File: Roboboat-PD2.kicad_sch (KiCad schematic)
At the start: 43 parts, among them J1 14.4V, J10 Motor, J11 Motor, J12 Motor, J13 Motor, J14 Motor, J15 Motor, J16 Motor, J17 GND TP, J2 PGOOD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

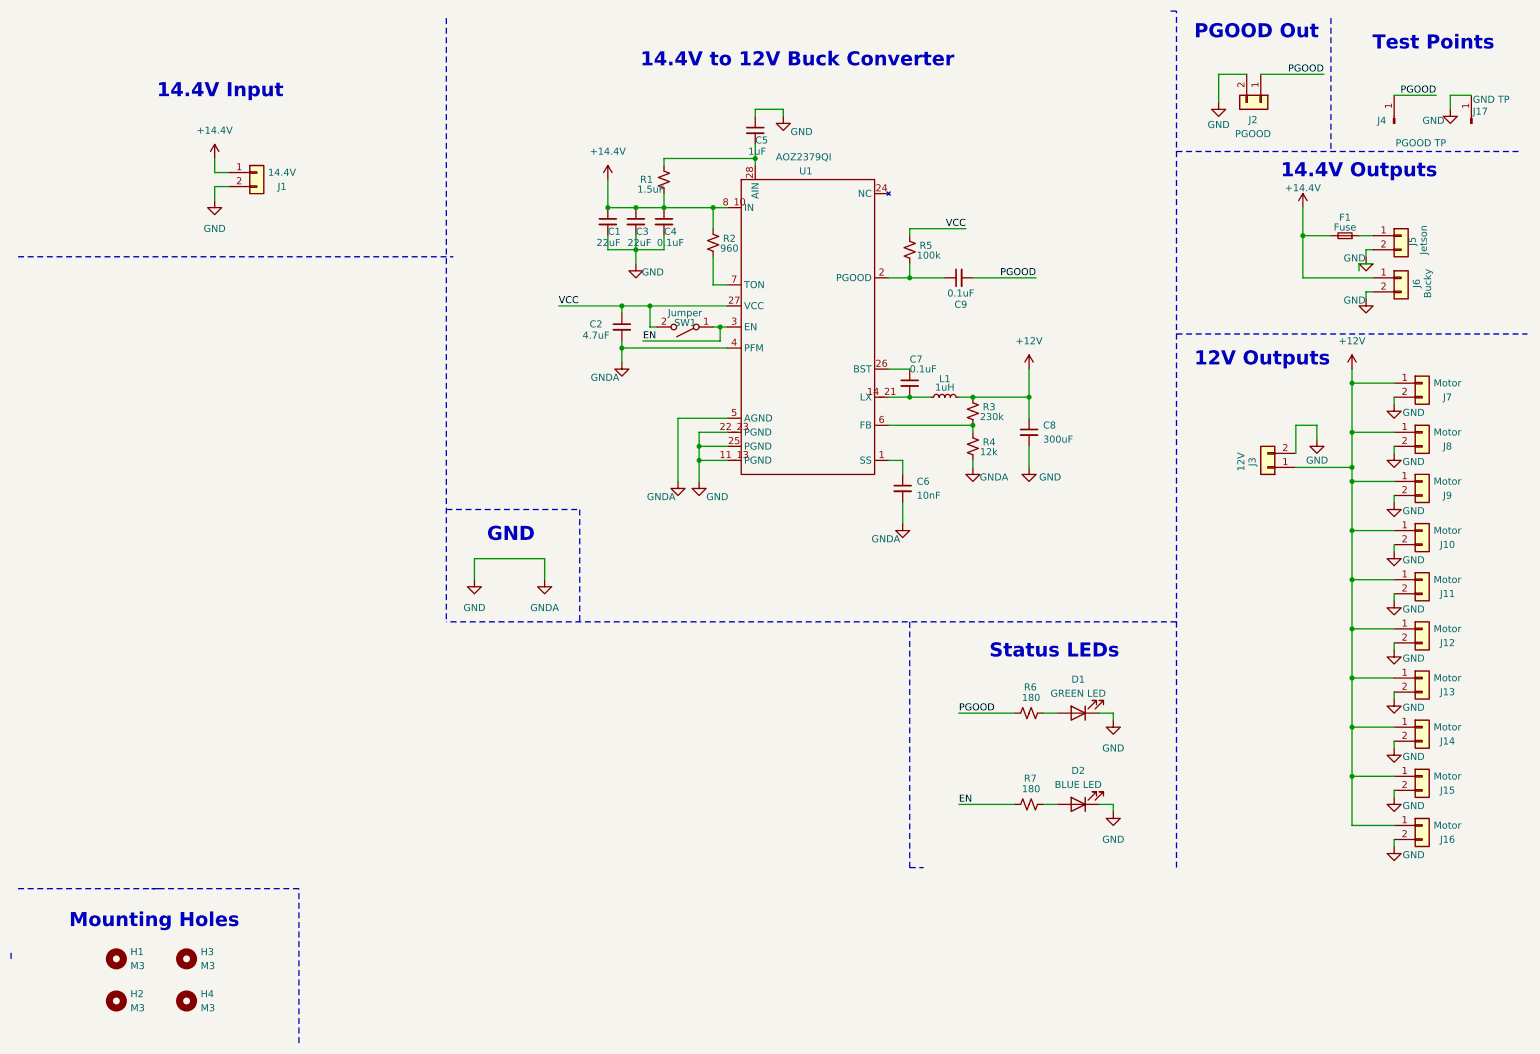
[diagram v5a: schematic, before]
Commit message: add more test points
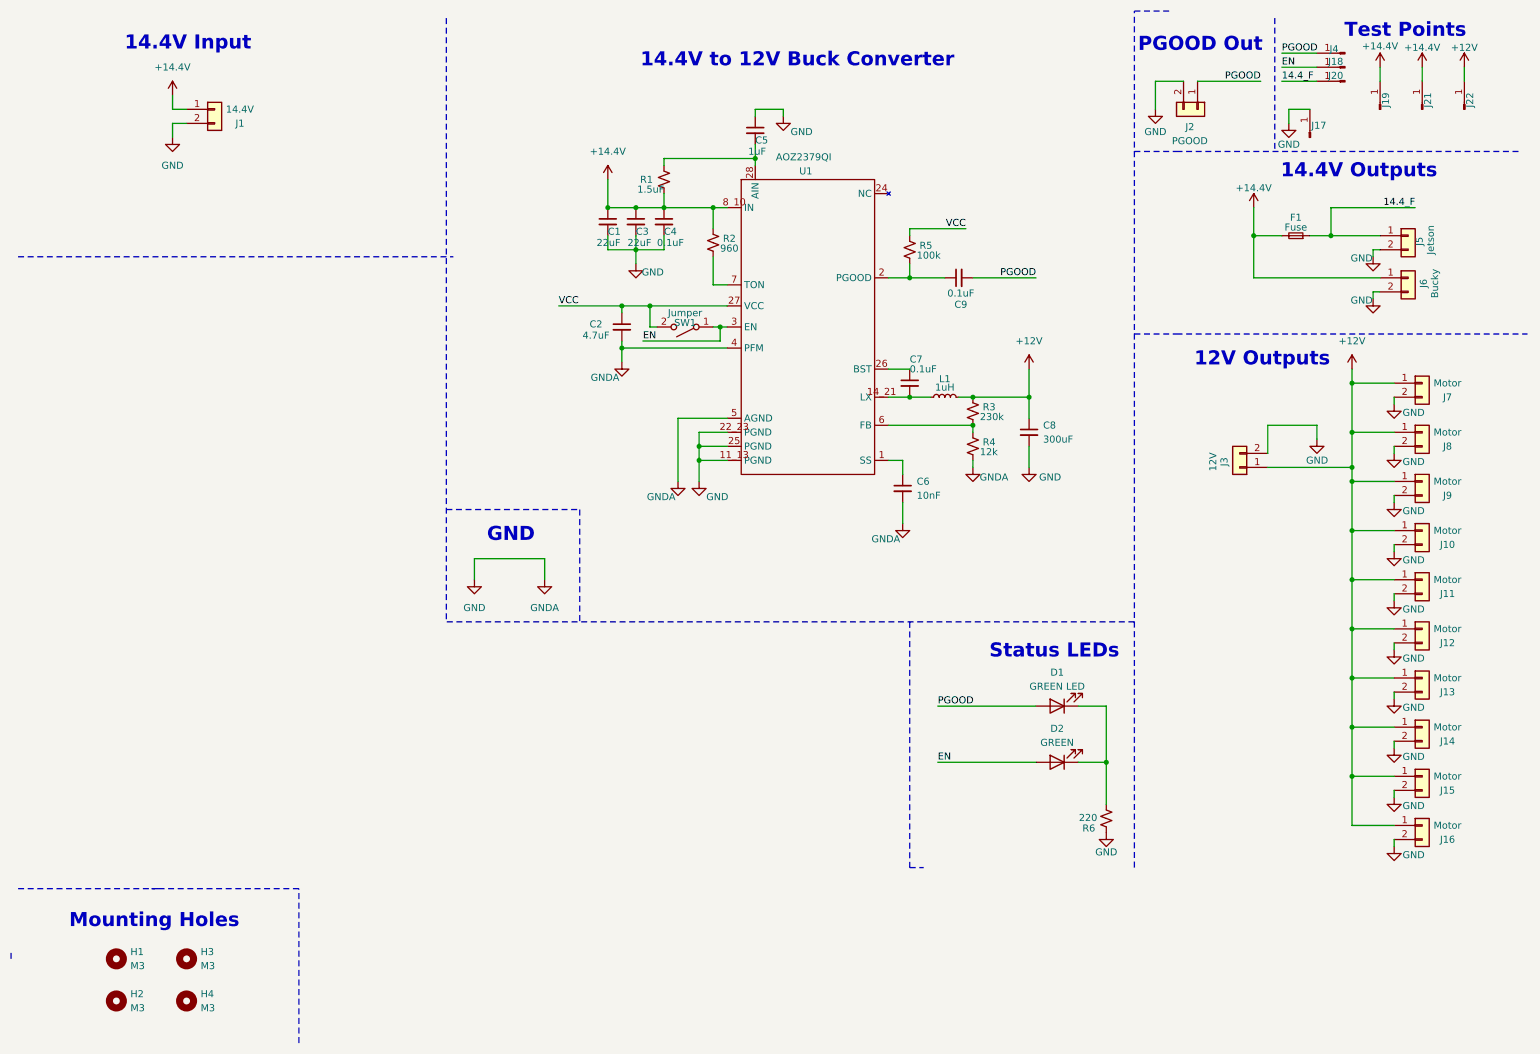
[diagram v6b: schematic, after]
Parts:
- removed R7: 180, Resistor_SMD:R_0805_2012Metric, symbol Device:R_Small_US
- added J18, J19, J20, J21, J22: PGOOD TP, TestPoint:TestPoint_Keystone_5000-5004_Miniature, symbol Connector:Conn_01x01_Pin
- D2: value BLUE LED -> GREEN
- J17, J4: footprint TestPoint:TestPoint_Keystone_5010-5014_Multipurpose -> TestPoint:TestPoint_Keystone_5000-5004_Miniature
- R6: value 180 -> 220
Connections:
- net +12V: now also J22.1 (Pin_1)
- net +14.4V: now also J19.1 (Pin_1), J21.1 (Pin_1)
- net EN: now also D2.2 (A), J18.1 (Pin_1)
- net GND: now also R6.2; no longer D1.1 (K), D2.1 (K)
- net PGOOD: now also D1.2 (A); no longer R6.1
- net 14.4_F: now reaches F1.1, J5.1 (Pin_1)
- net 14.4_F: now also J20.1 (Pin_1)
- new net: D1.1 (K), D2.1 (K), R6.1
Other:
- moved on the sheet: D1, D2, F1, J1, J17, J2, J3, J4, J5, J6

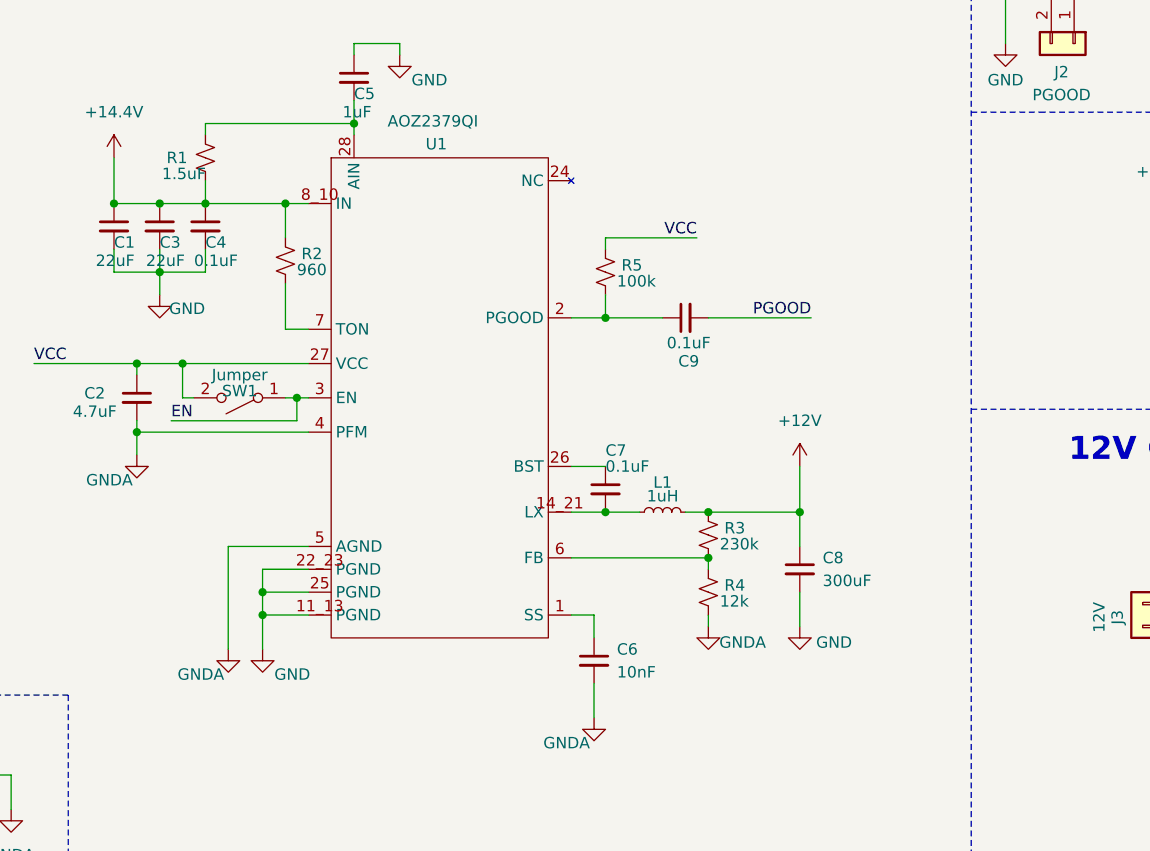
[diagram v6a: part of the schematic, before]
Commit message: correct buck converter component values
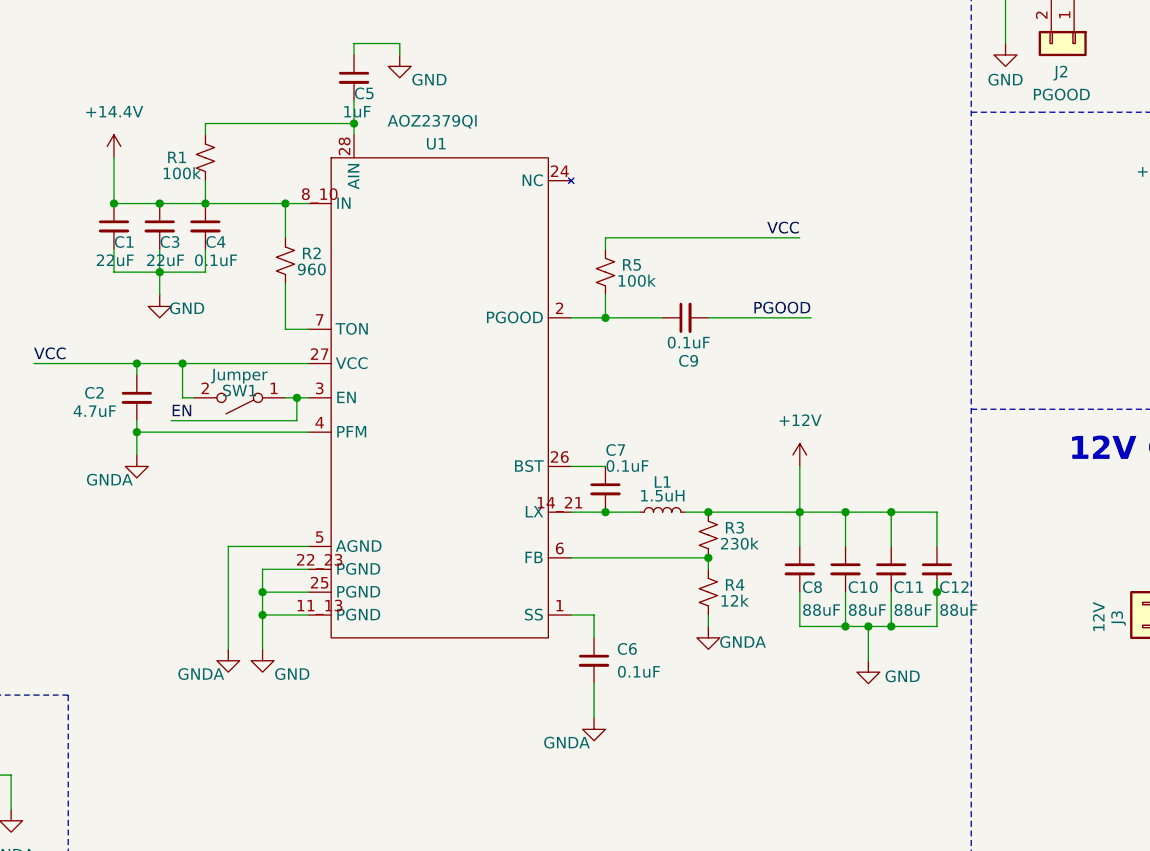
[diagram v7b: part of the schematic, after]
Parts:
- added C10, C11, C12: 88uF, Capacitor_SMD:C_0805_2012Metric, symbol Device:C_Small
- C6: value 10nF -> 0.1uF
- C8: value 300uF -> 88uF
- J6: footprint footprints:XT90_V -> Connector_AMASS:AMASS_XT60-M_1x02_P7.20mm_Vertical
- L1: value 1uH -> 1.5uH
- R1: value 1.5uF -> 100k
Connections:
- net +12V: now also C10.1, C11.1, C12.1
- net GND: now also C10.2, C11.2, C12.2

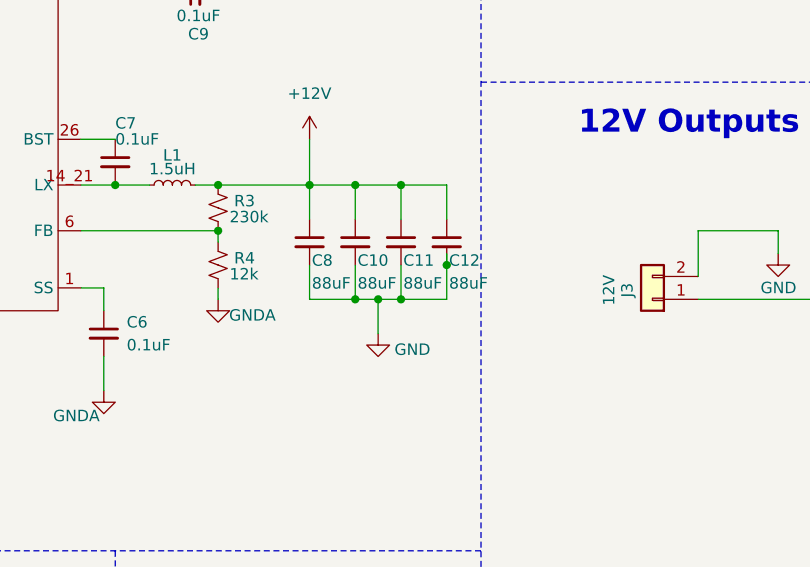
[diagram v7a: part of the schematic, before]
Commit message: use less thermal vias
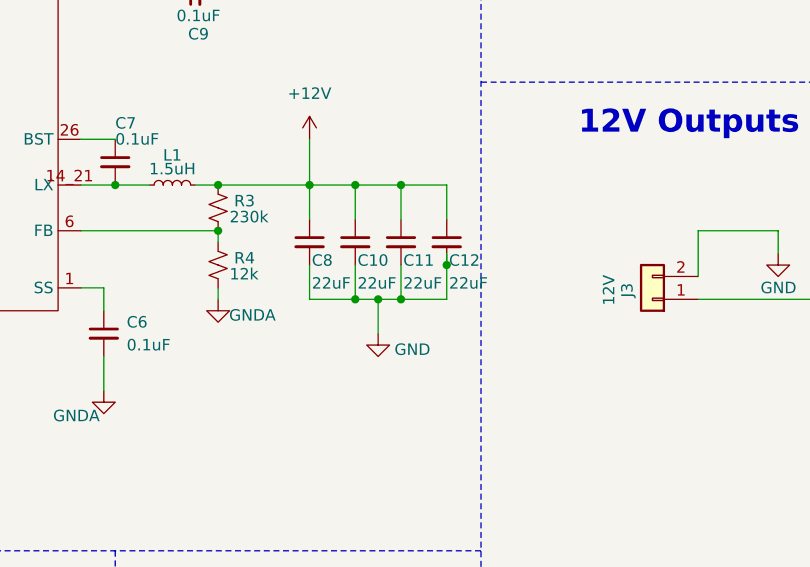
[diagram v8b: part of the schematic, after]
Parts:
- C10, C11, C12, C8: value 88uF -> 22uF
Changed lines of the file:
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@@
 			)
 		)
-		(property "Value" "88uF"
+		(property "Value" "22uF"
 			(at 195.834 92.202 0)
 			(effects
@@
 			)
 		)
-		(property "Value" "88uF"
+		(property "Value" "22uF"
 			(at 200.914 92.202 0)
 			(effects
@@
 			)
 		)
-		(property "Value" "88uF"
+		(property "Value" "22uF"
 			(at 211.074 92.202 0)
 			(effects
@@
 			)
 		)
-		(property "Value" "88uF"
+		(property "Value" "22uF"
 			(at 205.994 92.202 0)
 			(effects
